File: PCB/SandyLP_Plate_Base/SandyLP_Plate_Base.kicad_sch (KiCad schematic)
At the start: 0 parts

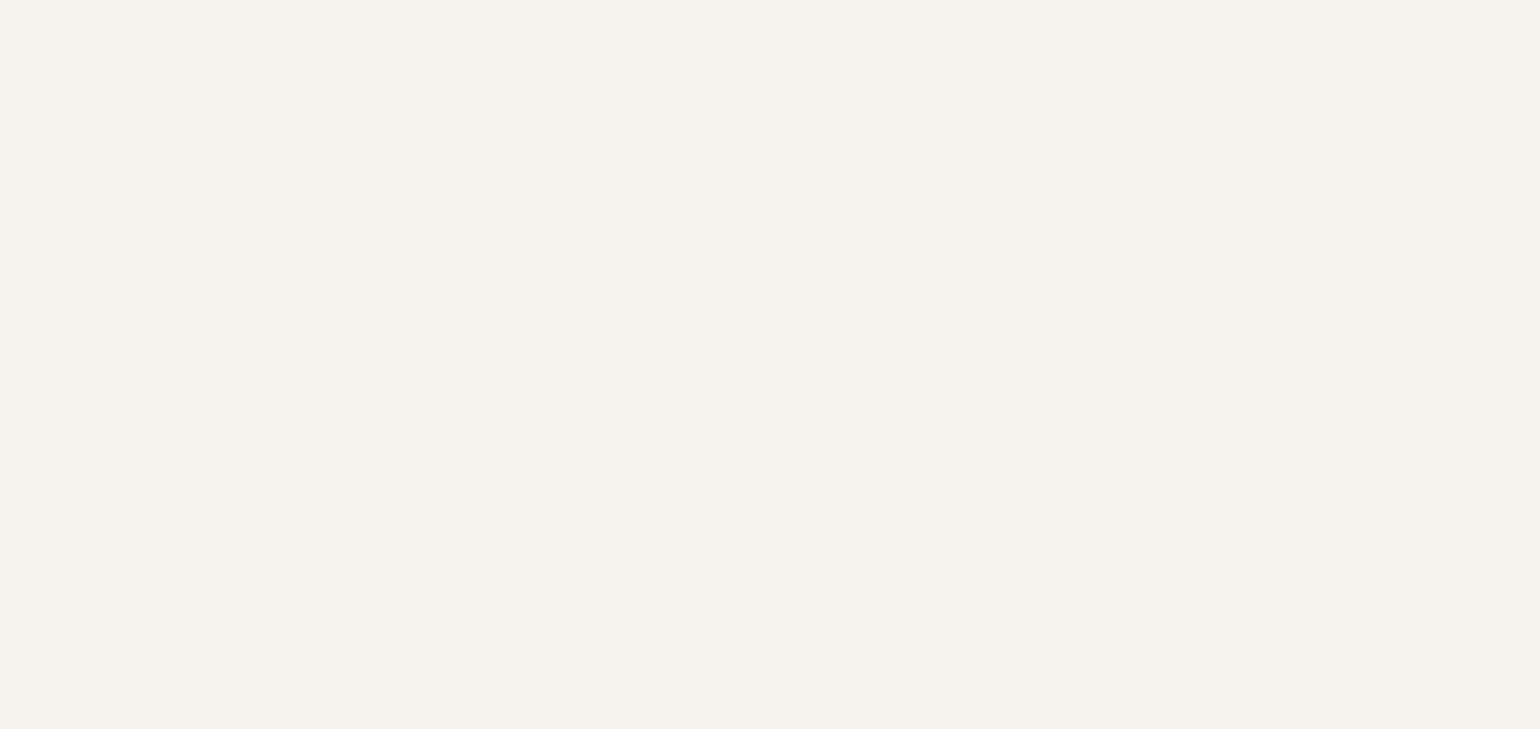
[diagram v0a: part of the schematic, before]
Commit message: 外形調整。スイッチ穴配置。
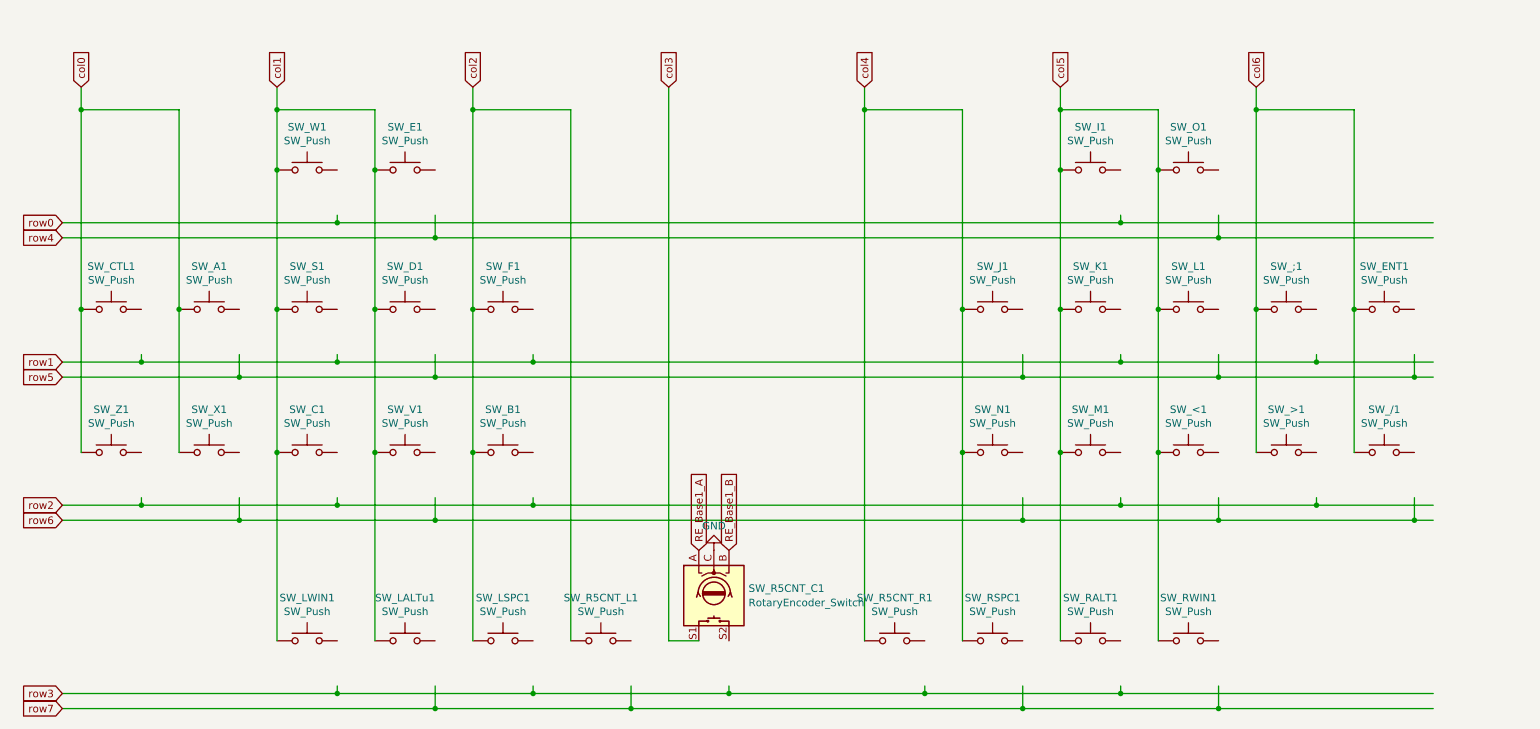
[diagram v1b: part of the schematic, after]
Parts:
- added SW_/1, SW_;1, SW_<1, SW_>1, SW_A1, SW_B1, SW_C1, SW_CTL1, SW_D1, SW_E1, SW_ENT1, SW_F1, SW_I1, SW_J1, SW_K1, SW_L1, SW_LALTu1, SW_LSPC1, SW_LWIN1, SW_M1, SW_N1, SW_O1, SW_R5CNT_L1, SW_R5CNT_R1, SW_RALT1, SW_RSPC1, SW_RWIN1, SW_S1, SW_V1, SW_W1, SW_X1, SW_Z1: SW_Push, locallib:MX-Switch-Hole-with-narrow-frame, symbol Switch:SW_Push
- added SW_R5CNT_C1: RotaryEncoder_Switch, locallib:MX-Switch-Hole-with-narrow-frame, symbol Device:RotaryEncoder_Switch
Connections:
- net GND: now also SW_R5CNT_C1.C
- new net RE_Base1_A: SW_R5CNT_C1.A
- new net RE_Base1_B: SW_R5CNT_C1.B
- new net col0: SW_A1.1, SW_CTL1.1, SW_X1.1, SW_Z1.1
- new net col1: SW_C1.1, SW_D1.1, SW_E1.1, SW_LALTu1.1, SW_LWIN1.1, SW_S1.1, SW_V1.1, SW_W1.1
- new net col2: SW_B1.1, SW_F1.1, SW_LSPC1.1, SW_R5CNT_L1.1
- new net col3: SW_R5CNT_C1.S1
- new net col4: SW_J1.1, SW_N1.1, SW_R5CNT_R1.1, SW_RSPC1.1
- new net col5: SW_<1.1, SW_I1.1, SW_K1.1, SW_L1.1, SW_M1.1, SW_O1.1, SW_RALT1.1, SW_RWIN1.1
- new net col6: SW_/1.1, SW_;1.1, SW_>1.1, SW_ENT1.1

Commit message: ロータリーエンコーダの穴サイズを縦に拡大
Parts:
- SW_R5CNT_C1: footprint locallib:MX-Switch-Hole-with-narrow-frame -> locallib:MX-Switch-Hole-for-RE(higher hole)-with-narrow-frame
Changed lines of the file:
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@@
 			)
 		)
-		(property "Footprint" "locallib:MX-Switch-Hole-with-narrow-frame"
+		(property "Footprint" "locallib:MX-Switch-Hole-for-RE(higher hole)-with-narrow-frame"
 			(at 137.541 109.22 0)
 			(effects
